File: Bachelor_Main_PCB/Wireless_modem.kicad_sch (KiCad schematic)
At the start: 45 parts, among them J10 JAE_SIM_Card_SF72S006, J12 M20-9990245, Q11 NX3008NBKW, Q5 NX3008NBKW, Q6 NX3008NBKW, Q7 NX3008NBKW, Q8 NX3008NBKW, Q9 NX3008NBKW, U2 RC7620_1104625, U5 ESD7004MUTAG

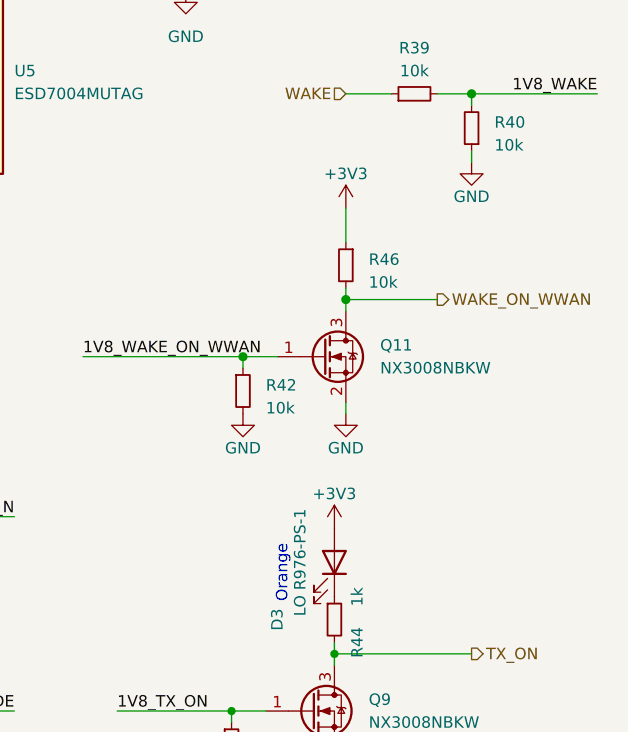
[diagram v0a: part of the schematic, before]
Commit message: Switched 3,3 for 3,5_MODEM for Q11 and Q9 circuits
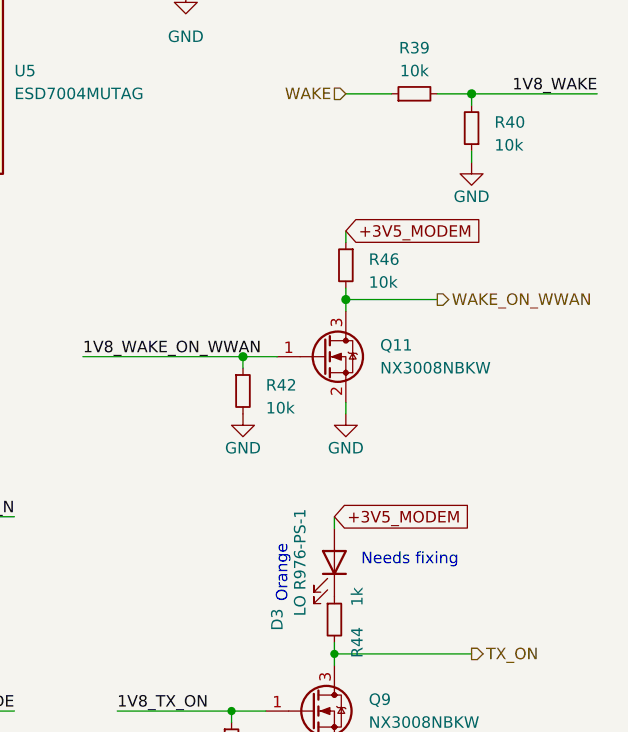
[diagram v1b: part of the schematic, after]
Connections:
- net +3V3 is gone; now on net +3V5_MODEM: D3.2 (A), R46.1
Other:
- note added: "Needs fixing"
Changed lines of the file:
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@@
 		)
 	)
+	(text "Needs fixing\n"
+		(exclude_from_sim no)
+		(at 262.382 134.366 0)
+		(effects
+			(font
+				(size 1.27 1.27)
+			)
+		)
+	)
 	(text "WIRELESS MODEM power jumper"
 		(exclude_from_sim no)
@@
 	(wire
 		(pts
+			(xy 255.27 97.79) (xy 255.27 99.06)
+		)
+		(stroke
+			(width 0)
+			(type default)
+		)
+	)
+	(wire
+		(pts
 			(xy 243.84 46.99) (xy 227.33 46.99)
 		)
@@
 	(wire
 		(pts
+			(xy 254 129.54) (xy 254 130.81)
+		)
+		(stroke
+			(width 0)
+			(type default)
+		)
+	)
+	(wire
+		(pts
 			(xy 181.61 114.3) (xy 185.42 114.3)
 		)
@@
 	(wire
 		(pts
-			(xy 255.27 99.06) (xy 255.27 95.25)
-		)
-		(stroke
-			(width 0)
-			(type default)
-		)
-	)
-	(wire
-		(pts
 			(xy 180.34 33.02) (xy 198.12 33.02)
 		)
@@
 	(global_label "+3V5_MODEM"
 		(shape input)
+		(at 255.27 97.79 0)
+		(fields_autoplaced yes)
+		(effects
+			(font
+				(size 1.27 1.27)
+			)
+			(justify left)
+		)
+		(property "Intersheetrefs" "${INTERSHEET_REFS}"
+			(at 270.9551 97.79 0)
+			(effects
+				(font
+					(size 1.27 1.27)
+				)
+				(justify left)
+				(hide yes)
+			)
+		)
+	)
+	(global_label "+3V5_MODEM"
+		(shape input)
 		(at 52.07 69.85 180)
 		(fields_autoplaced yes)
@@
 	(global_label "+3V5_MODEM"
 		(shape input)
+		(at 254 129.54 0)
+		(fields_autoplaced yes)
+		(effects
+			(font
+				(size 1.27 1.27)
+			)
+			(justify left)
+		)
+		(property "Intersheetrefs" "${INTERSHEET_REFS}"
+			(at 269.6851 129.54 0)
+			(effects
+				(font
+					(size 1.27 1.27)
+				)
+				(justify left)
+				(hide yes)
+			)
+		)
+	)
+	(global_label "+3V5_MODEM"
+		(shape input)
 		(at 140.97 176.53 0)
 		(fields_autoplaced yes)
@@
 					(unit 1)
 				)
-			)
-		)
-	)
-	(symbol
-		(lib_id "power:+3V3")
-		(at 255.27 95.25 0)
-		(mirror y)
-		(unit 1)
-		(exclude_from_sim no)
-		(in_bom yes)
-		(on_board yes)
-		(dnp no)
-		(fields_autoplaced yes)
-		(property "Reference" "#PWR0155"
-			(at 255.27 99.06 0)
-			(effects
-				(font
-					(size 1.27 1.27)
-				)
-				(hide yes)
-			)
-		)
-		(property "Value" "+3V3"
-			(at 255.27 91.44 0)
-			(effects
-				(font
-					(size 1.27 1.27)
-				)
-			)
-		)
-		(property "Footprint" ""
-			(at 255.27 95.25 0)
-			(effects
-				(font
-					(size 1.27 1.27)
-				)
-				(hide yes)
-			)
-		)
-		(property "Datasheet" ""
-			(at 255.27 95.25 0)
-			(effects
-				(font
-					(size 1.27 1.27)
-				)
-				(hide yes)
-			)
-		)
-		(property "Description" ""
-			(at 255.27 95.25 0)
-			(effects
-				(font
-					(size 1.27 1.27)
-				)
-				(hide yes)
-			)
-		)
-		(pin "1"
-		)
-		(instances
-			(project "Bachelor_Main_PCB"
-				(path "/3544d663-329e-4884-b753-28436ca187e8/0bbef2a3-1d79-4cf0-b531-d6abf690b331"
-					(reference "#PWR0155")
-					(unit 1)
-				)
-			)
-		)
-	)
-	(symbol
-		(lib_id "power:+3V3")
-		(at 254 130.81 0)
-		(mirror y)
-		(unit 1)
-		(exclude_from_sim no)
-		(in_bom yes)
-		(on_board yes)
-		(dnp no)
-		(fields_autoplaced yes)
-		(property "Reference" "#PWR0153"
-			(at 254 134.62 0)
-			(effects
-				(font
-					(size 1.27 1.27)
-				)
-				(hide yes)
-			)
-		)
-		(property "Value" "+3V3"
-			(at 254 127 0)
-			(effects
-				(font
-					(size 1.27 1.27)
-				)
-			)
-		)
-		(property "Footprint" ""
-			(at 254 130.81 0)
-			(effects
-				(font
-					(size 1.27 1.27)
-				)
-				(hide yes)
-			)
-		)
-		(property "Datasheet" ""
-			(at 254 130.81 0)
-			(effects
-				(font
-					(size 1.27 1.27)
-				)
-				(hide yes)
-			)
-		)
-		(property "Description" ""
-			(at 254 130.81 0)
-			(effects
-				(font
-					(size 1.27 1.27)
-				)
-				(hide yes)
-			)
-		)
-		(pin "1"
-		)
-		(instances
-			(project "Bachelor_Main_PCB"
-				(path "/3544d663-329e-4884-b753-28436ca187e8/0bbef2a3-1d79-4cf0-b531-d6abf690b331"
-					(reference "#PWR0153")
-					(unit 1)
-				)

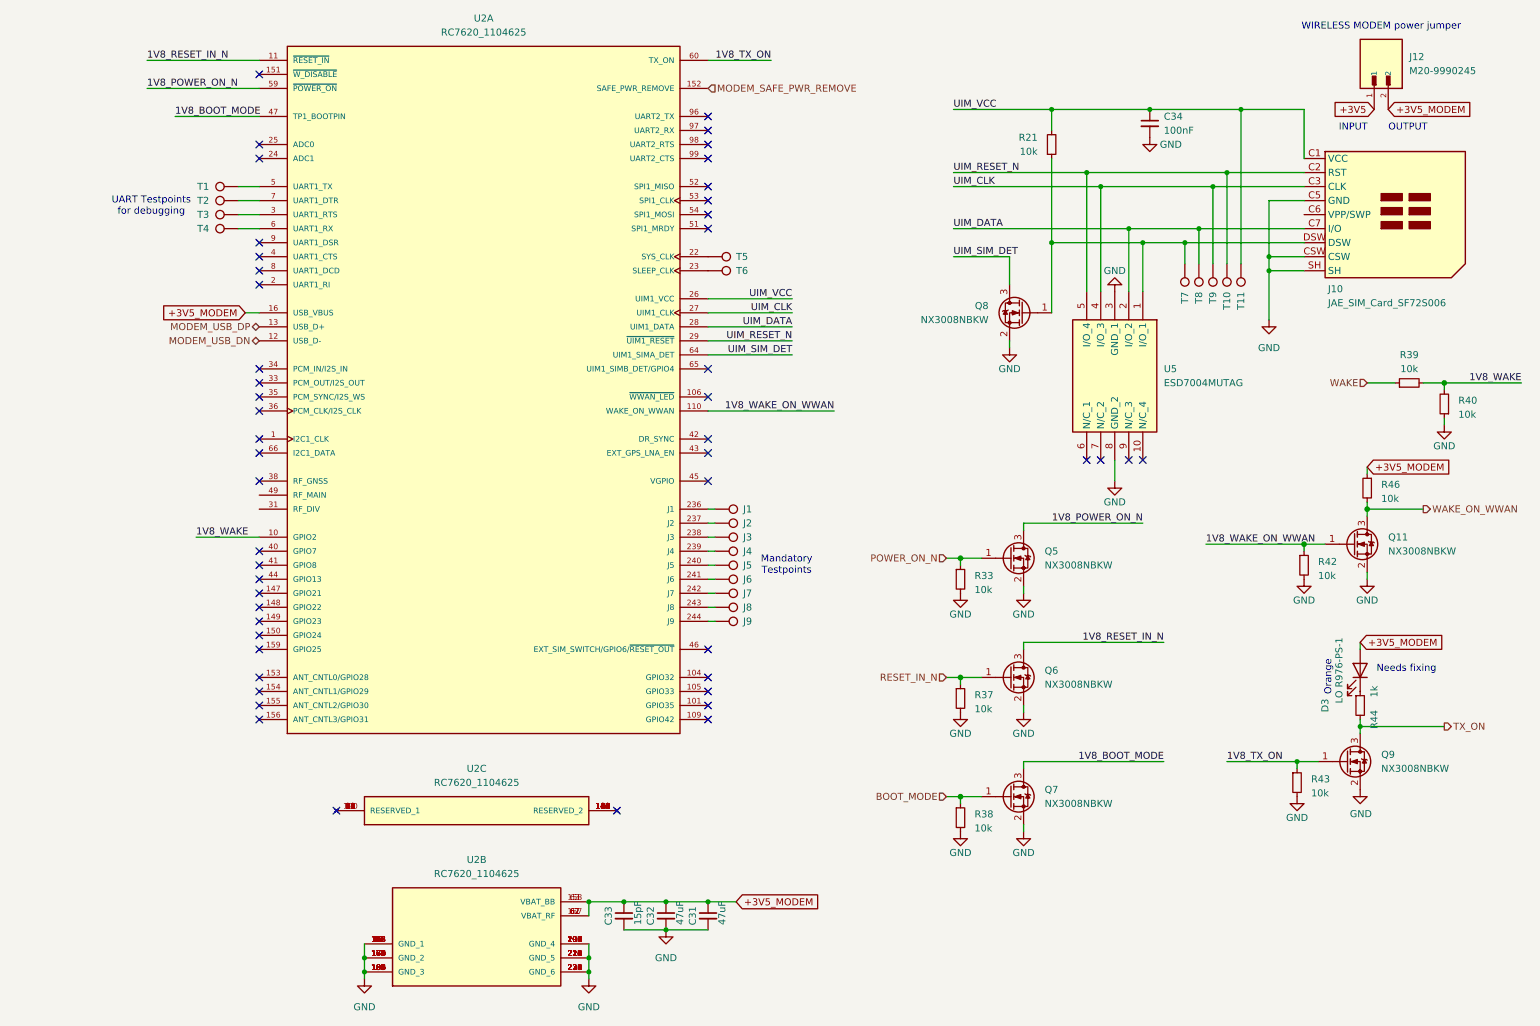
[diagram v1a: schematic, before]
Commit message: Add MODEM_3V5_EN mosfet
Controlls the power supply to the modem from the RPI GPIO7
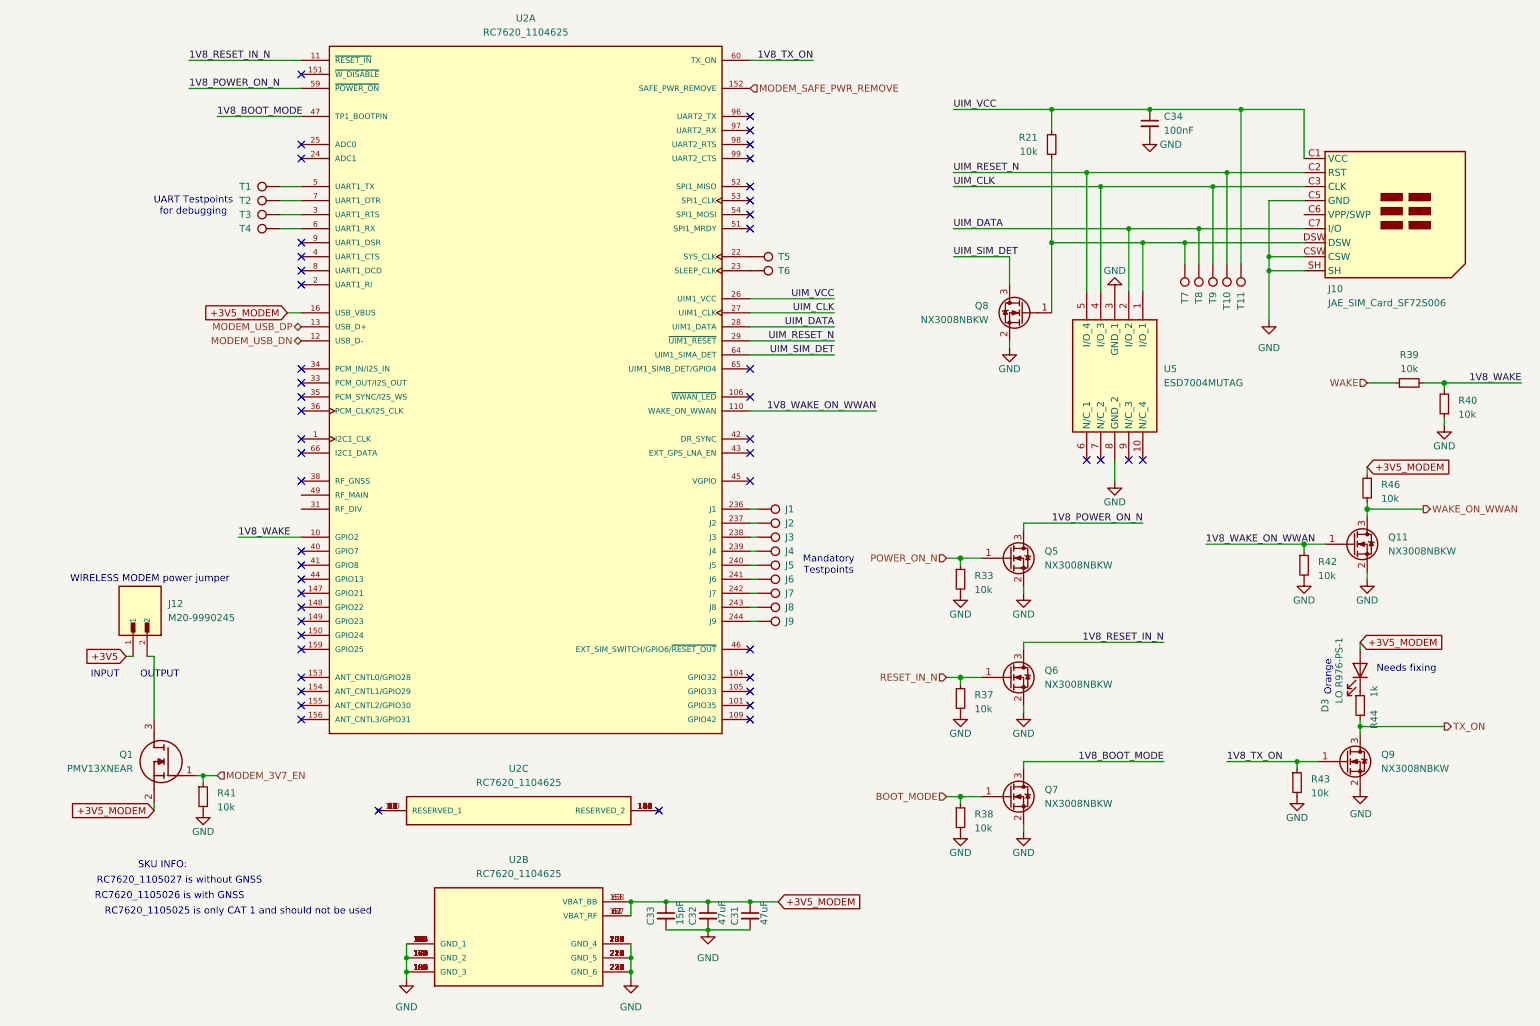
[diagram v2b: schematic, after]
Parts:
- added Q1: PMV13XNEAR, KiCad3:SOT95P230X110-3N, symbol PMV13XNEAR:PMV13XNEAR
- added R41: 10k, Resistor_SMD:R_0402_1005Metric, symbol Device:R_Small
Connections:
- net +3V5_MODEM: now also Q1.2 (S); no longer J12.2
- net GND: now also R41.2
- new net: J12.2, Q1.3 (D)
- new net MODEM_3V7_EN: Q1.1 (G), R41.1
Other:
- note added: "RC7620_1105025 is only CAT 1 and should not be used"
- note added: "RC7620_1105026 is with GNSS"
- note added: "RC7620_1105027 is without GNSS"
- note added: "SKU INFO:"
- moved on the sheet: C31, C32, C33, J1, J12, J2, J3, J4, J5, J6, J7, J8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

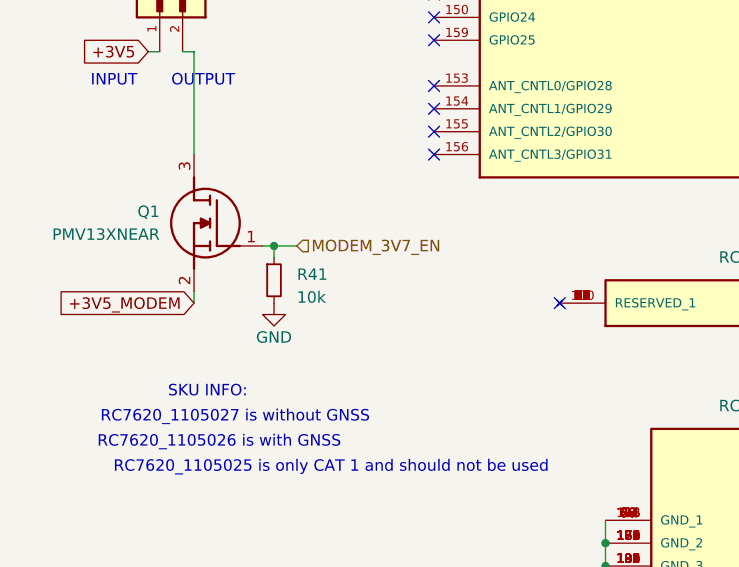
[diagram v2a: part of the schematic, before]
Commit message: Change MODEM_3V5_EN mosfet to P-channel type SSM3j358R
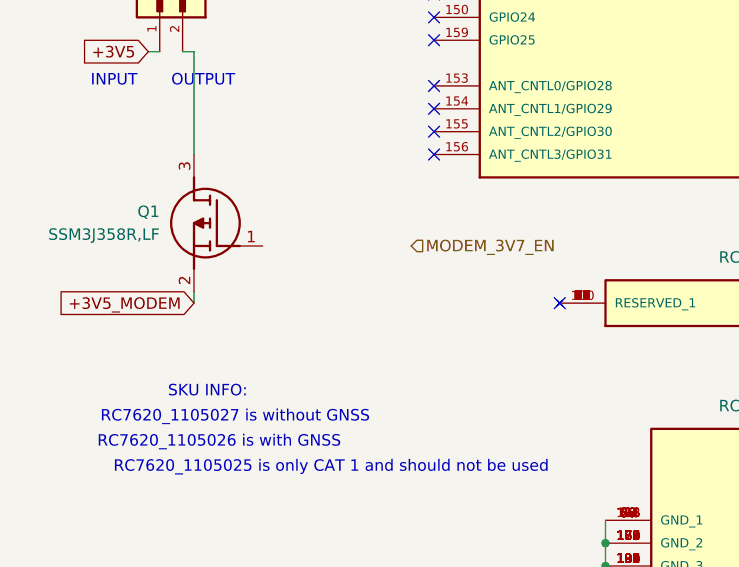
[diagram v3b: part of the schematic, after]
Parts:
- removed Q1: PMV13XNEAR, KiCad3:SOT95P230X110-3N, symbol PMV13XNEAR:PMV13XNEAR
- removed R41: 10k, Resistor_SMD:R_0402_1005Metric, symbol Device:R_Small
- added Q1: SSM3J358R,LF, KiCad4:SOTFL95P240X88-3N, symbol SSM3J358R_LF:SSM3J358R,LF
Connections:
- net +3V5_MODEM: now also Q1.2 (S)
- net at J12.2: now also Q1.3 (D)

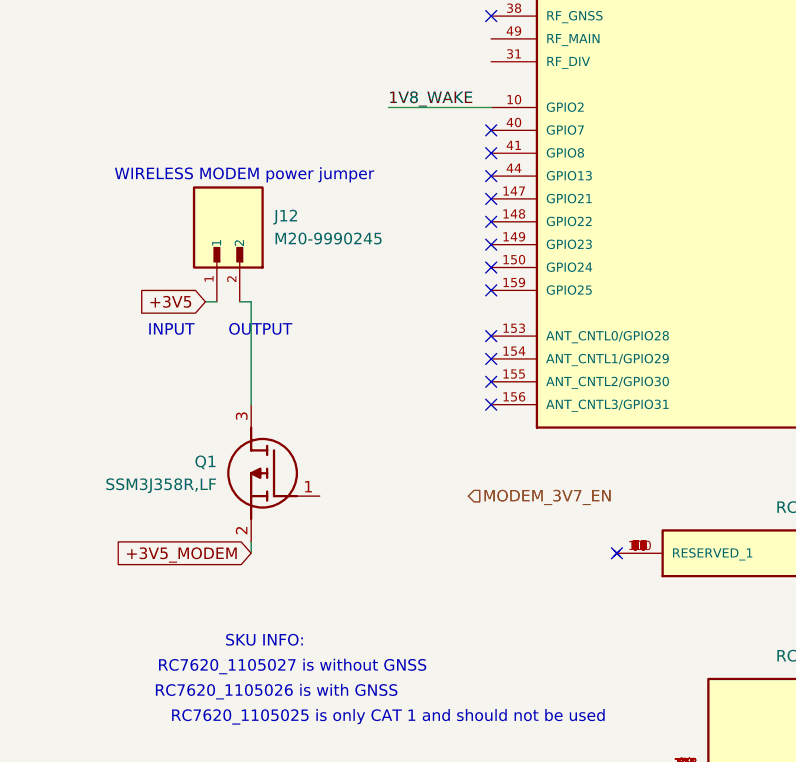
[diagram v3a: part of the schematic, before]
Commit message: ADD MODEM_3V5_EN signal inverter
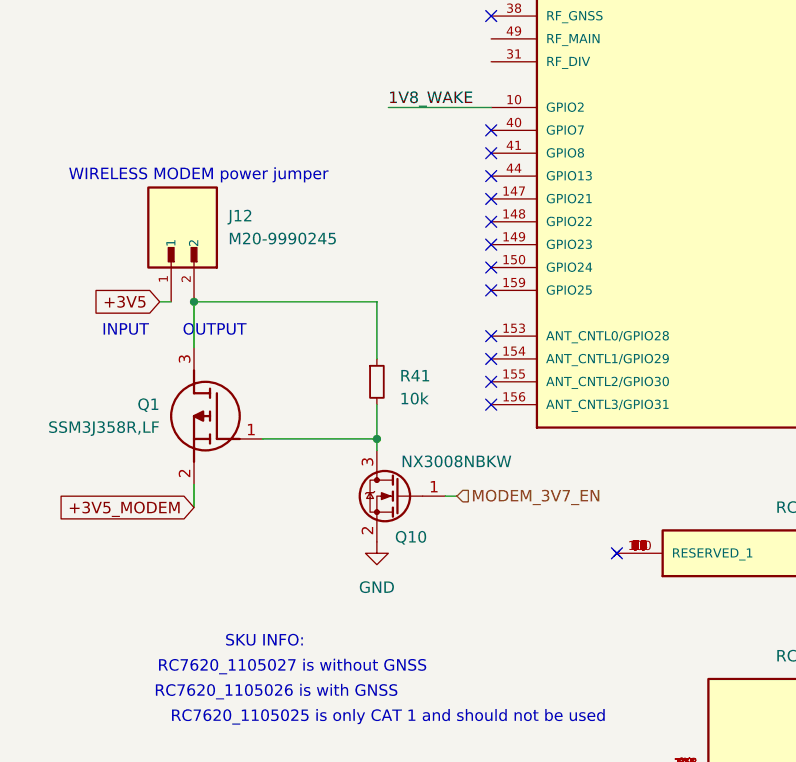
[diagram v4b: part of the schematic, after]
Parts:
- added Q10: NX3008NBKW, Package_TO_SOT_SMD:SOT-323_SC-70, symbol Device:Q_NMOS_GSD
- added R41: 10k, Resistor_SMD:R_0402_1005Metric, symbol Device:R_Small
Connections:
- net GND: now also Q10.2 (S)
- net MODEM_3V7_EN: now also Q10.1 (G)
- net at J12.2, Q1.3 (D): now also R41.1
- net at Q1.1 (G): now also Q10.3 (D), R41.2
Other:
- moved on the sheet: J12, Q1

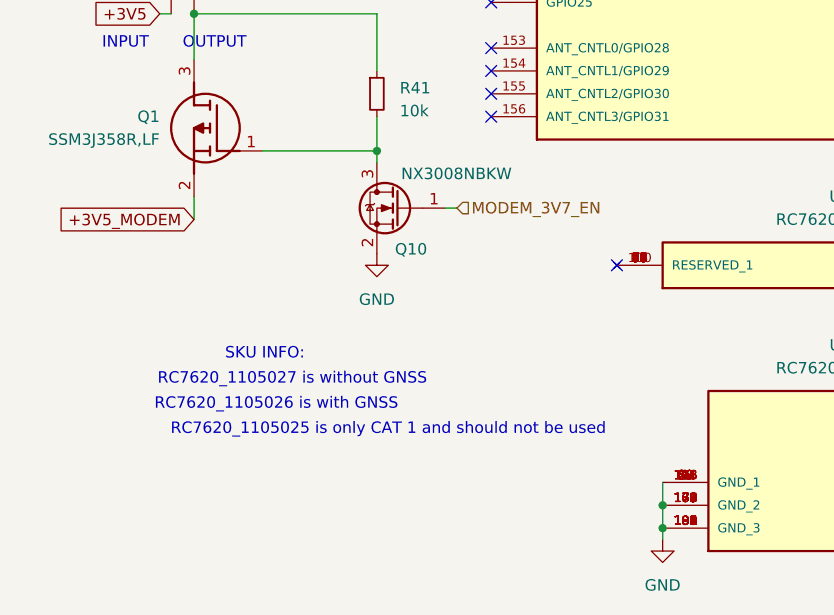
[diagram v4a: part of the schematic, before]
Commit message: Renamed wring MODEM_3V7_en to 3V5
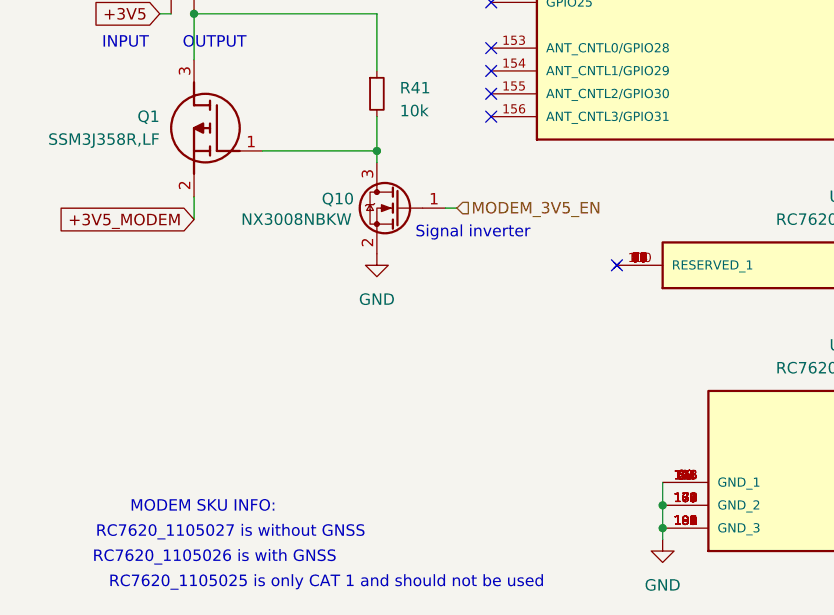
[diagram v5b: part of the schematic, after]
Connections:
- net MODEM_3V7_EN renamed MODEM_3V5_EN
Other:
- note added: "MODEM SKU INFO:"
- note added: "Signal inverter"
- note removed: "SKU INFO:"
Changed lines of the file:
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@@
 	(text "RC7620_1105026 is with GNSS"
 		(exclude_from_sim no)
-		(at 38.354 175.514 0)
+		(at 31.496 192.532 0)
 		(effects
 			(font
@@
 	(text "RC7620_1105025 is only CAT 1 and should not be used"
 		(exclude_from_sim no)
-		(at 50.8 178.308 0)
+		(at 43.942 195.326 0)
 		(effects
 			(font
@@
 		)
 	)
-	(text "SKU INFO:"
+	(text "MODEM SKU INFO:"
 		(exclude_from_sim no)
-		(at 37.084 169.926 0)
+		(at 30.226 186.944 0)
+		(effects
+			(font
+				(size 1.27 1.27)
+			)
+		)
+	)
+	(text "Signal inverter"
+		(exclude_from_sim no)
+		(at 60.198 156.464 0)
 		(effects
 			(font
@@
 	(text "RC7620_1105027 is without GNSS"
 		(exclude_from_sim no)
-		(at 40.132 172.72 0)
+		(at 33.274 189.738 0)
 		(effects
 			(font
@@
 		)
 	)
-	(hierarchical_label "MODEM_3V7_EN"
+	(hierarchical_label "MODEM_3V5_EN"
 		(shape input)
 		(at 58.42 153.67 0)
@@
 		(dnp no)
 		(property "Reference" "Q10"
-			(at 55.118 158.242 0)
+			(at 46.99 152.654 0)
 			(effects
 				(font
@@
 		)
 		(property "Value" "NX3008NBKW"
-			(at 64.516 149.86 0)
+			(at 46.736 154.94 0)
 			(effects
 				(font

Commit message: Routed Sheeets
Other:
- note added: "Potential use pin. not used on BUGG"
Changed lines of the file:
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@@
+		)
+	)
+	(text "Potential use pin. not used on BUGG"
+		(exclude_from_sim no)
+		(at 161.29 27.686 0)
+		(effects
+			(font
+				(size 1.27 1.27)
+			)
 		)
 	)
